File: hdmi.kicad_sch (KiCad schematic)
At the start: 6 parts, among them J3501 FPC0.5-SMT-20P, U3501 RCLAMP0524P, U3502 RCLAMP0524P, U3503 RCLAMP0524P

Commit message: Fix schematic ERC errors
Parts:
- U3501, U3502, U3503: footprint Package_SON:USON-10_2.5x1.0mm_P0.5mm -> Package_DFN_QFN:Diodes_UDFN-10_1.0x2.5mm_P0.5mm; symbol Yellow:TPD4EUSB30 -> Hatlabs:RCLAMP0524P
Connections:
- net HDMI.CEC: no longer U3501.6 (D2-)
- net HDMI.CLK+: no longer U3502.10 (D1+)
- net HDMI.CLK-: no longer U3502.9 (D1-)
- net HDMI.D0+: no longer U3502.7 (D2+)
- net HDMI.D0-: no longer U3502.6 (D2-)
- net HDMI.D1+: no longer U3503.10 (D1+)
- net HDMI.D1-: no longer U3503.9 (D1-)
- net HDMI.D2+: no longer U3503.7 (D2+)
- net HDMI.D2-: no longer U3503.6 (D2-)
- net HDMI.HPD: no longer U3501.10 (D1+)
- net HDMI.SCL: no longer U3501.7 (D2+)
- net HDMI.SDA: no longer U3501.9 (D1-)
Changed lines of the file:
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@@
-			)
-		)
-		(property "Sim.Enable" ""
-			(at 162.56 120.65 0)
-			(effects
-				(font
-					(size 1.27 1.27)
-				)
 			)
 		)
@@
 	)
 	(symbol
-		(lib_name "Power_Protection:TPD4EUSB30_1")
-		(lib_id "Yellow:TPD4EUSB30")
+		(lib_id "Hatlabs:RCLAMP0524P")
 		(at 95.25 105.41 0)
 		(unit 1)
@@
 			)
 		)
-		(property "Footprint" "Package_SON:USON-10_2.5x1.0mm_P0.5mm"
+		(property "Footprint" "Package_DFN_QFN:Diodes_UDFN-10_1.0x2.5mm_P0.5mm"
 			(at 71.12 115.57 0)
 			(effects
@@
 			)
 		)
-		(property "Description" ""
+		(property "Description" "4-Channel Low Capacitance TVS Diode Array, DFN-10"
 			(at 95.25 105.41 0)
 			(effects
@@
 			)
 		)
-		(property "Sim.Enable" ""
-			(at 95.25 105.41 0)
-			(effects
-				(font
-					(size 1.27 1.27)
-				)
-			)
-		)
 		(pin "1"
 		)
@@
 	)
 	(symbol
-		(lib_name "Power_Protection:TPD4EUSB30_1")
-		(lib_id "Yellow:TPD4EUSB30")
+		(lib_id "Hatlabs:RCLAMP0524P")
 		(at 95.25 72.39 0)
 		(unit 1)
@@
 			)
 		)
-		(property "Footprint" "Package_SON:USON-10_2.5x1.0mm_P0.5mm"
+		(property "Footprint" "Package_DFN_QFN:Diodes_UDFN-10_1.0x2.5mm_P0.5mm"
 			(at 71.12 82.55 0)
 			(effects
@@
 			)
 		)
-		(property "Description" ""
+		(property "Description" "4-Channel Low Capacitance TVS Diode Array, DFN-10"
 			(at 95.25 72.39 0)
 			(effects
@@
 		)
 		(property "Component Class" "fine_pitch"
-			(at 95.25 72.39 0)
-			(effects
-				(font
-					(size 1.27 1.27)
-				)
-			)
-		)
-		(property "Sim.Enable" ""
 			(at 95.25 72.39 0)
 			(effects
@@
 			)
 		)
-		(property "Sim.Enable" ""
-			(at 195.58 93.98 0)
-			(effects
-				(font
-					(size 1.27 1.27)
-				)
-			)
-		)
 		(pin "12"
 		)
@@
 	)
 	(symbol
-		(lib_name "Power_Protection:TPD4EUSB30_1")
-		(lib_id "Yellow:TPD4EUSB30")
+		(lib_id "Hatlabs:RCLAMP0524P")
 		(at 95.25 138.43 0)
 		(unit 1)
@@
 			)
 		)
-		(property "Footprint" "Package_SON:USON-10_2.5x1.0mm_P0.5mm"
+		(property "Footprint" "Package_DFN_QFN:Diodes_UDFN-10_1.0x2.5mm_P0.5mm"
 			(at 71.12 148.59 0)
 			(effects
@@
 			)
 		)
-		(property "Description" ""
+		(property "Description" "4-Channel Low Capacitance TVS Diode Array, DFN-10"
 			(at 95.25 138.43 0)
 			(effects
@@
 		)
 		(property "Component Class" "fine_pitch"
-			(at 95.25 138.43 0)
-			(effects
-				(font
-					(size 1.27 1.27)
-				)
-			)
-		)
-		(property "Sim.Enable" ""
 			(at 95.25 138.43 0)
 			(effects
@@
 			)
 		)
-		(property "Sim.Enable" ""
-			(at 156.21 113.03 0)
-			(effects
-				(font
-					(size 1.27 1.27)
-				)
-			)
-		)

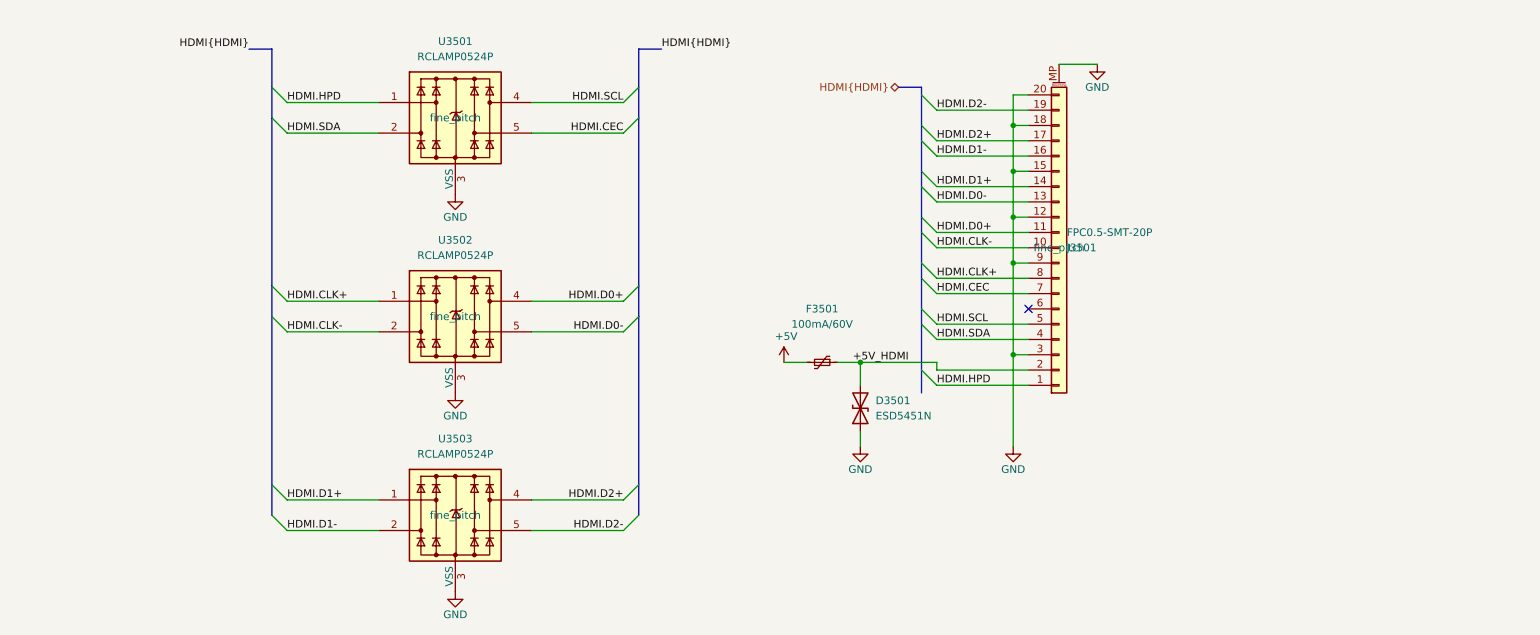
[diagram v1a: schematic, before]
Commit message: Reannotate components
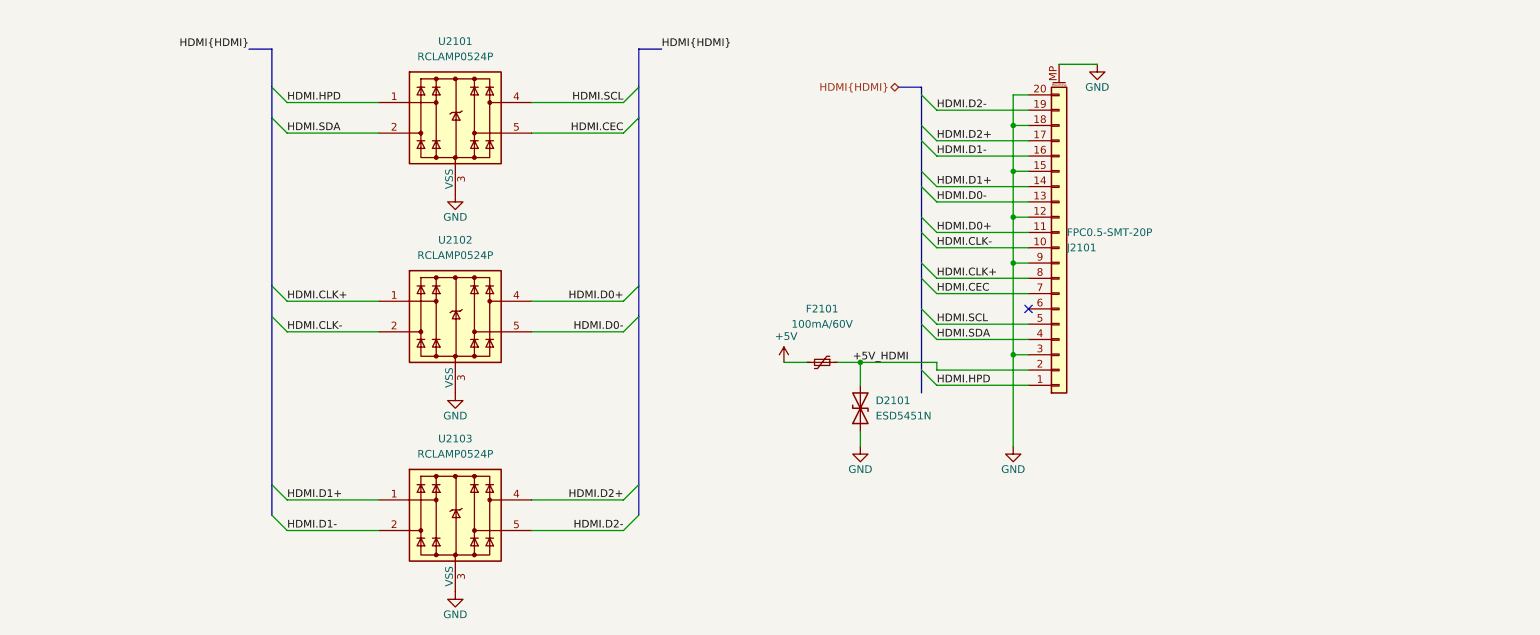
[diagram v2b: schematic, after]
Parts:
- renumbered D3501 to D2101, F3501 to F2101, J3501 to J2101, U3501 to U2101, U3502 to U2102, U3503 to U2103
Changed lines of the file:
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@@
 		(dnp no)
 		(fields_autoplaced yes)
-		(property "Reference" "D3501"
+		(property "Reference" "D2101"
 			(at 165.1 119.3799 90)
 			(effects
@@
 			(project "HALPI2"
 				(path "/abc482bd-3f17-4d35-80db-1da3dcdb5c27/851e7ce4-d5b0-47f7-ace9-4a347f172348/49314faa-db35-4ef5-b0c8-5c327f44891d"
-					(reference "D3501")
-					(unit 1)
-				)
-				(path "/abc482bd-3f17-4d35-80db-1da3dcdb5c27/851e7ce4-d5b0-47f7-ace9-4a347f172348/890900ed-b859-477a-afc8-e6aecd491b67"
-					(reference "D3701")
+					(reference "D2201")
+					(unit 1)
+				)
+				(path "/abc482bd-3f17-4d35-80db-1da3dcdb5c27/851e7ce4-d5b0-47f7-ace9-4a347f172348/890900ed-b859-477a-afc8-e6aecd491b67"
+					(reference "D2101")
 					(unit 1)
 				)
@@
 		(on_board yes)
 		(dnp no)
-		(property "Reference" "#PWR03506"
+		(property "Reference" "#PWR02107"
 			(at 201.93 69.85 0)
 			(effects
@@
 			(project "HALPI2"
 				(path "/abc482bd-3f17-4d35-80db-1da3dcdb5c27/851e7ce4-d5b0-47f7-ace9-4a347f172348/49314faa-db35-4ef5-b0c8-5c327f44891d"
-					(reference "#PWR03506")
-					(unit 1)
-				)
-				(path "/abc482bd-3f17-4d35-80db-1da3dcdb5c27/851e7ce4-d5b0-47f7-ace9-4a347f172348/890900ed-b859-477a-afc8-e6aecd491b67"
-					(reference "#PWR03603")
+					(reference "#PWR02207")
+					(unit 1)
+				)
+				(path "/abc482bd-3f17-4d35-80db-1da3dcdb5c27/851e7ce4-d5b0-47f7-ace9-4a347f172348/890900ed-b859-477a-afc8-e6aecd491b67"
+					(reference "#PWR02107")
 					(unit 1)
 				)
@@
 		(on_board yes)
 		(dnp no)
-		(property "Reference" "#PWR03505"
+		(property "Reference" "#PWR02106"
 			(at 187.96 133.35 0)
 			(effects
@@
 			(project "HALPI2"
 				(path "/abc482bd-3f17-4d35-80db-1da3dcdb5c27/851e7ce4-d5b0-47f7-ace9-4a347f172348/49314faa-db35-4ef5-b0c8-5c327f44891d"
-					(reference "#PWR03505")
-					(unit 1)
-				)
-				(path "/abc482bd-3f17-4d35-80db-1da3dcdb5c27/851e7ce4-d5b0-47f7-ace9-4a347f172348/890900ed-b859-477a-afc8-e6aecd491b67"
-					(reference "#PWR03602")
+					(reference "#PWR02206")
+					(unit 1)
+				)
+				(path "/abc482bd-3f17-4d35-80db-1da3dcdb5c27/851e7ce4-d5b0-47f7-ace9-4a347f172348/890900ed-b859-477a-afc8-e6aecd491b67"
+					(reference "#PWR02106")
 					(unit 1)
 				)
@@
 		(on_board yes)
 		(dnp no)
-		(property "Reference" "U3502"
+		(property "Reference" "U2102"
 			(at 95.25 92.71 0)
 			(effects
@@
 					(size 1.27 1.27)
 				)
+				(hide yes)
 			)
 		)
@@
 			(project "HALPI2"
 				(path "/abc482bd-3f17-4d35-80db-1da3dcdb5c27/851e7ce4-d5b0-47f7-ace9-4a347f172348/49314faa-db35-4ef5-b0c8-5c327f44891d"
-					(reference "U3502")
-					(unit 1)
-				)
-				(path "/abc482bd-3f17-4d35-80db-1da3dcdb5c27/851e7ce4-d5b0-47f7-ace9-4a347f172348/890900ed-b859-477a-afc8-e6aecd491b67"
-					(reference "U3602")
+					(reference "U2202")
+					(unit 1)
+				)
+				(path "/abc482bd-3f17-4d35-80db-1da3dcdb5c27/851e7ce4-d5b0-47f7-ace9-4a347f172348/890900ed-b859-477a-afc8-e6aecd491b67"
+					(reference "U2102")
 					(unit 1)
 				)
@@
 		(on_board yes)
 		(dnp no)
-		(property "Reference" "U3501"
+		(property "Reference" "U2101"
 			(at 95.25 59.69 0)
 			(effects
@@
 					(size 1.27 1.27)
 				)
+				(hide yes)
 			)
 		)
@@
 			(project "HALPI2"
 				(path "/abc482bd-3f17-4d35-80db-1da3dcdb5c27/851e7ce4-d5b0-47f7-ace9-4a347f172348/49314faa-db35-4ef5-b0c8-5c327f44891d"
-					(reference "U3501")
-					(unit 1)
-				)
-				(path "/abc482bd-3f17-4d35-80db-1da3dcdb5c27/851e7ce4-d5b0-47f7-ace9-4a347f172348/890900ed-b859-477a-afc8-e6aecd491b67"
-					(reference "U3601")
+					(reference "U2201")
+					(unit 1)
+				)
+				(path "/abc482bd-3f17-4d35-80db-1da3dcdb5c27/851e7ce4-d5b0-47f7-ace9-4a347f172348/890900ed-b859-477a-afc8-e6aecd491b67"
+					(reference "U2101")
 					(unit 1)
 				)
@@
 		(on_board yes)
 		(dnp no)
-		(property "Reference" "#PWR03507"
+		(property "Reference" "#PWR02105"
 			(at 162.56 133.35 0)
 			(effects
@@
 			(project "HALPI2"
 				(path "/abc482bd-3f17-4d35-80db-1da3dcdb5c27/851e7ce4-d5b0-47f7-ace9-4a347f172348/49314faa-db35-4ef5-b0c8-5c327f44891d"
-					(reference "#PWR03507")
-					(unit 1)
-				)
-				(path "/abc482bd-3f17-4d35-80db-1da3dcdb5c27/851e7ce4-d5b0-47f7-ace9-4a347f172348/890900ed-b859-477a-afc8-e6aecd491b67"
-					(reference "#PWR03701")
+					(reference "#PWR02205")
+					(unit 1)
+				)
+				(path "/abc482bd-3f17-4d35-80db-1da3dcdb5c27/851e7ce4-d5b0-47f7-ace9-4a347f172348/890900ed-b859-477a-afc8-e6aecd491b67"
+					(reference "#PWR02105")
 					(unit 1)
 				)
@@
 		(on_board yes)
 		(dnp no)
-		(property "Reference" "#PWR03501"
+		(property "Reference" "#PWR02101"
 			(at 95.25 91.44 0)
 			(effects
@@
 			(project "HALPI2"
 				(path "/abc482bd-3f17-4d35-80db-1da3dcdb5c27/851e7ce4-d5b0-47f7-ace9-4a347f172348/49314faa-db35-4ef5-b0c8-5c327f44891d"
-					(reference "#PWR03501")
-					(unit 1)
-				)
-				(path "/abc482bd-3f17-4d35-80db-1da3dcdb5c27/851e7ce4-d5b0-47f7-ace9-4a347f172348/890900ed-b859-477a-afc8-e6aecd491b67"
-					(reference "#PWR03604")
+					(reference "#PWR02201")
+					(unit 1)
+				)
+				(path "/abc482bd-3f17-4d35-80db-1da3dcdb5c27/851e7ce4-d5b0-47f7-ace9-4a347f172348/890900ed-b859-477a-afc8-e6aecd491b67"
+					(reference "#PWR02101")
 					(unit 1)
 				)
@@
 		(on_board yes)
 		(dnp no)
-		(property "Reference" "#PWR03504"
+		(property "Reference" "#PWR02104"
 			(at 149.86 116.84 0)
 			(effects
@@
 			(project "HALPI2"
 				(path "/abc482bd-3f17-4d35-80db-1da3dcdb5c27/851e7ce4-d5b0-47f7-ace9-4a347f172348/49314faa-db35-4ef5-b0c8-5c327f44891d"
-					(reference "#PWR03504")
-					(unit 1)
-				)
-				(path "/abc482bd-3f17-4d35-80db-1da3dcdb5c27/851e7ce4-d5b0-47f7-ace9-4a347f172348/890900ed-b859-477a-afc8-e6aecd491b67"
-					(reference "#PWR03601")
+					(reference "#PWR02204")
+					(unit 1)
+				)
+				(path "/abc482bd-3f17-4d35-80db-1da3dcdb5c27/851e7ce4-d5b0-47f7-ace9-4a347f172348/890900ed-b859-477a-afc8-e6aecd491b67"
+					(reference "#PWR02104")
 					(unit 1)
 				)
@@
 		(on_board yes)
 		(dnp no)
-		(property "Reference" "J3501"
+		(property "Reference" "J2101"
 			(at 196.85 93.9801 0)
 			(effects
@@
 					(size 1.27 1.27)
 				)
+				(hide yes)
 			)
 		)
@@
 			(project "HALPI2"
 				(path "/abc482bd-3f17-4d35-80db-1da3dcdb5c27/851e7ce4-d5b0-47f7-ace9-4a347f172348/49314faa-db35-4ef5-b0c8-5c327f44891d"
-					(reference "J3501")
-					(unit 1)
-				)
-				(path "/abc482bd-3f17-4d35-80db-1da3dcdb5c27/851e7ce4-d5b0-47f7-ace9-4a347f172348/890900ed-b859-477a-afc8-e6aecd491b67"
-					(reference "J3601")
+					(reference "J2201")
+					(unit 1)
+				)
+				(path "/abc482bd-3f17-4d35-80db-1da3dcdb5c27/851e7ce4-d5b0-47f7-ace9-4a347f172348/890900ed-b859-477a-afc8-e6aecd491b67"
+					(reference "J2101")
 					(unit 1)
 				)
@@
 		(on_board yes)
 		(dnp no)
-		(property "Reference" "#PWR03502"
+		(property "Reference" "#PWR02102"
 			(at 95.25 124.46 0)
 			(effects
@@
 			(project "HALPI2"
 				(path "/abc482bd-3f17-4d35-80db-1da3dcdb5c27/851e7ce4-d5b0-47f7-ace9-4a347f172348/49314faa-db35-4ef5-b0c8-5c327f44891d"
-					(reference "#PWR03502")
-					(unit 1)
-				)
-				(path "/abc482bd-3f17-4d35-80db-1da3dcdb5c27/851e7ce4-d5b0-47f7-ace9-4a347f172348/890900ed-b859-477a-afc8-e6aecd491b67"
-					(reference "#PWR03605")
+					(reference "#PWR02202")
+					(unit 1)
+				)
+				(path "/abc482bd-3f17-4d35-80db-1da3dcdb5c27/851e7ce4-d5b0-47f7-ace9-4a347f172348/890900ed-b859-477a-afc8-e6aecd491b67"
+					(reference "#PWR02102")
 					(unit 1)
 				)
@@
 		(on_board yes)
 		(dnp no)
-		(property "Reference" "#PWR03503"
+		(property "Reference" "#PWR02103"
 			(at 95.25 157.48 0)
 			(effects
@@
 			(project "HALPI2"
 				(path "/abc482bd-3f17-4d35-80db-1da3dcdb5c27/851e7ce4-d5b0-47f7-ace9-4a347f172348/49314faa-db35-4ef5-b0c8-5c327f44891d"
-					(reference "#PWR03503")
-					(unit 1)
-				)
-				(path "/abc482bd-3f17-4d35-80db-1da3dcdb5c27/851e7ce4-d5b0-47f7-ace9-4a347f172348/890900ed-b859-477a-afc8-e6aecd491b67"
-					(reference "#PWR03606")
+					(reference "#PWR02203")
+					(unit 1)
+				)
+				(path "/abc482bd-3f17-4d35-80db-1da3dcdb5c27/851e7ce4-d5b0-47f7-ace9-4a347f172348/890900ed-b859-477a-afc8-e6aecd491b67"
+					(reference "#PWR02103")
 					(unit 1)
 				)
@@
 		(on_board yes)
 		(dnp no)
-		(property "Reference" "U3503"
+		(property "Reference" "U2103"
 			(at 95.25 125.73 0)
 			(effects
@@
 					(size 1.27 1.27)
 				)
+				(hide yes)
 			)
 		)
@@
 			(project "HALPI2"
 				(path "/abc482bd-3f17-4d35-80db-1da3dcdb5c27/851e7ce4-d5b0-47f7-ace9-4a347f172348/49314faa-db35-4ef5-b0c8-5c327f44891d"
-					(reference "U3503")
-					(unit 1)
-				)
-				(path "/abc482bd-3f17-4d35-80db-1da3dcdb5c27/851e7ce4-d5b0-47f7-ace9-4a347f172348/890900ed-b859-477a-afc8-e6aecd491b67"
-					(reference "U3603")
+					(reference "U2203")
+					(unit 1)
+				)
+				(path "/abc482bd-3f17-4d35-80db-1da3dcdb5c27/851e7ce4-d5b0-47f7-ace9-4a347f172348/890900ed-b859-477a-afc8-e6aecd491b67"
+					(reference "U2103")
 					(unit 1)
 				)
@@
 		(dnp no)
 		(fields_autoplaced yes)
-		(property "Reference" "F3501"
+		(property "Reference" "F2101"
 			(at 156.21 104.14 90)
 			(effects
@@
 			(project "HALPI2"
 				(path "/abc482bd-3f17-4d35-80db-1da3dcdb5c27/851e7ce4-d5b0-47f7-ace9-4a347f172348/49314faa-db35-4ef5-b0c8-5c327f44891d"
-					(reference "F3501")
-					(unit 1)
-				)
-				(path "/abc482bd-3f17-4d35-80db-1da3dcdb5c27/851e7ce4-d5b0-47f7-ace9-4a347f172348/890900ed-b859-477a-afc8-e6aecd491b67"
-					(reference "F3601")
-					(unit 1)
-				)
+					(reference "F2201")
+					(unit 1)
+				)
+				(path "/abc482bd-3f17-4d35-80db-1da3dcdb5c27/851e7ce4-d5b0-47f7-ace9-4a347f172348/890900ed-b859-477a-afc8-e6aecd491b67"
+					(reference "F2101")
+					(unit 1)
+				)

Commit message: Most DRC errors fixed
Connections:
- net HDMI.CEC: now also U2101.6 (NC)
- net HDMI.CLK+: now also U2102.10 (NC)
- net HDMI.CLK-: now also U2102.9 (NC)
- net HDMI.D0+: now also U2102.7 (NC)
- net HDMI.D0-: now also U2102.6 (NC)
- net HDMI.D1+: now also U2103.10 (NC)
- net HDMI.D1-: now also U2103.9 (NC)
- net HDMI.D2+: now also U2103.7 (NC)
- net HDMI.D2-: now also U2103.6 (NC)
- net HDMI.HPD: now also U2101.10 (NC)
- net HDMI.SCL: now also U2101.7 (NC)
- net HDMI.SDA: now also U2101.9 (NC)

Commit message: Further refinements
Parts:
- removed F2101: 100mA/60V, Fuse:Fuse_1206_3216Metric, symbol Device:Polyfuse_Small
- added C3104, C3106: 10uF, Capacitor_SMD:C_0805_2012Metric, symbol Device:C_Small
- added C3105: 1uF, Capacitor_SMD:C_0402_1005Metric, symbol Device:C_Small
- added R3102: 49.9k, Resistor_SMD:R_0603_1608Metric, symbol Device:R_Small
- added TP3102: TestPoint, TestPoint:TestPoint_Pad_D1.0mm, symbol Connector:TestPoint
- added U3102: AP22653W6-7, Package_TO_SOT_SMD:SOT-23-6, symbol Hatlabs:AP22653
- J2101: LCSC C2914144 -> C11073
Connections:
- net +5V: now also C3104.1, C3105.1, U3102.1 (IN)
- net +5V_HDMI: now also C3106.1, TP3102.1, U3102.6 (OUT)
- net GND: now also C3104.2, C3105.2, C3106.2, R3102.1, U3102.2 (GND)
- new net ILIM: R3102.2, U3102.5 (ILIM)
- new net SD.PWR: U3102.3 (EN)
- no-connect marks 1 -> 2
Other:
- note added: "Current limiting"
- note added: "Note that the FFC connector pin numbering is reversed relative to HDMI pinout."
- moved on the sheet: D2101, J2101, U2101, U2102, U2103
